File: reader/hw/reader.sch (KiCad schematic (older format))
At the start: 35 parts, among them P101 Wago_233-502, P102 Wago_233-502, P103 CONN_02X05, P104 JST, P105 CONN_01X08, Q101 MMBT2222A, Q102 MMBT2222A, U101 LP2992AIM5-3.3CT-ND, U102 SN75176BDR, U103 MKE04P24M48SF0, X101 CRYSTAL

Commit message: Restructure files and small updates
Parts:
- added R112: R, smd-handsolder:R_1206_HandSoldering, symbol R
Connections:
- wire segments 110 -> 113
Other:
- note added: "PTA3 is open drain output, external pull-up might be\nnecessary see Figure 11-2 in the Kinetis KEO4Z\nuser manual.\n\nBut the input of SN75176 is pulled up internally so\nin this case the resistor is probably not needed. \nSee Figure 19 of TI's sn75176b.pdf\n\nI am keeping the R here just in case it is needed\nfor reliable operation."
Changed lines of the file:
@@
 Text Label 6900 3350 0    60   ~ 0
 IRQ
+$Comp
+L +3.3V #PWR041
+U 1 1 59272043
+P 7000 5000
+F 0 "#PWR041" H 7000 4850 50  0001 C CNN
+F 1 "+3.3V" V 7015 5128 50  0000 L CNN
+F 2 "" H 7000 5000 60  0000 C CNN
+F 3 "" H 7000 5000 60  0000 C CNN
+	1    7000 5000
+	0    -1   -1   0
+$EndComp
+$Comp
+L R R112
+U 1 1 5927213E
+P 7200 5000
+F 0 "R112" V 7300 5000 50  0000 C CNN
+F 1 "R" V 7200 5000 50  0000 C CNN
+F 2 "smd-handsolder:R_1206_HandSoldering" V 7130 5000 30  0001 C CNN
+F 3 "" H 7200 5000 30  0000 C CNN
+	1    7200 5000
+	0    -1   1    0
+$EndComp
+Wire Wire Line
+	7350 5000 7400 5000
+Wire Wire Line
+	7400 5000 7400 4650
+Connection ~ 7400 4650
+Wire Wire Line
+	7000 5000 7050 5000
+Text Notes 5200 6100 0    60   ~ 0
+PTA3 is open drain output, external pull-up might be\nnecessary see Figure 11-2 in the Kinetis KEO4Z\nuser manual.\n\nBut the input of SN75176 is pulled up internally so\nin this case the resistor is probably not needed. \nSee Figure 19 of TI's sn75176b.pdf\n\nI am keeping the R here just in case it is needed\nfor reliable operation.
 $EndSCHEMATC

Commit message: Fix voltage for SPI flash, short under one capacitor
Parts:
- U103: symbol MKE04P24M48SF0 -> MKE04P24M48SF0-RESCUE-reader
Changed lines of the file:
@@
 EESchema Schematic File Version 2
+LIBS:reader-rescue
 LIBS:capacitors
 LIBS:connectors
@@
 $EndDescr
 $Comp
-L MKE04P24M48SF0 U103
+L MKE04P24M48SF0-RESCUE-reader U103
 U 1 1 591A19D8
 P 5850 3950

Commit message: New KiCAD lib references, crystal feedback R, basic uart impl
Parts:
- added R?: 10M, symbol simple:R
- C101, C102, C103, C104, C106, C107, C108, C109, C111: symbol C -> simple:C
- C105, C110: symbol Jamicon_220uF_16V_TKP -> capacitors:Jamicon_220uF_16V_TKP
- D101, D102: symbol LED -> simple:LED
- P101, P102: symbol Wago_233-502 -> connectors:Wago_233-502
- P103: symbol CONN_02X05 -> connectors:CONN_02X05
- P104: symbol CONN_01X02 -> connectors:CONN_01X02
- P105: symbol CONN_01X08 -> connectors:CONN_01X08
- Q101, Q102: symbol MMBT2222A -> transistors:MMBT2222A
- R101, R102, R103, R104, R105, R106, R107, R108, R109, R110, R111, R112: symbol R -> simple:R
- U101: symbol LP2992AIM5-3.3CT-ND -> power:LP2992AIM5-3.3CT-ND
- U102: symbol SN75176BDR -> ic:SN75176BDR
- U103: symbol MKE04P24M48SF0-RESCUE-reader -> reader-rescue:MKE04P24M48SF0-RESCUE-reader
- X101: symbol CRYSTAL -> templates:CRYSTAL

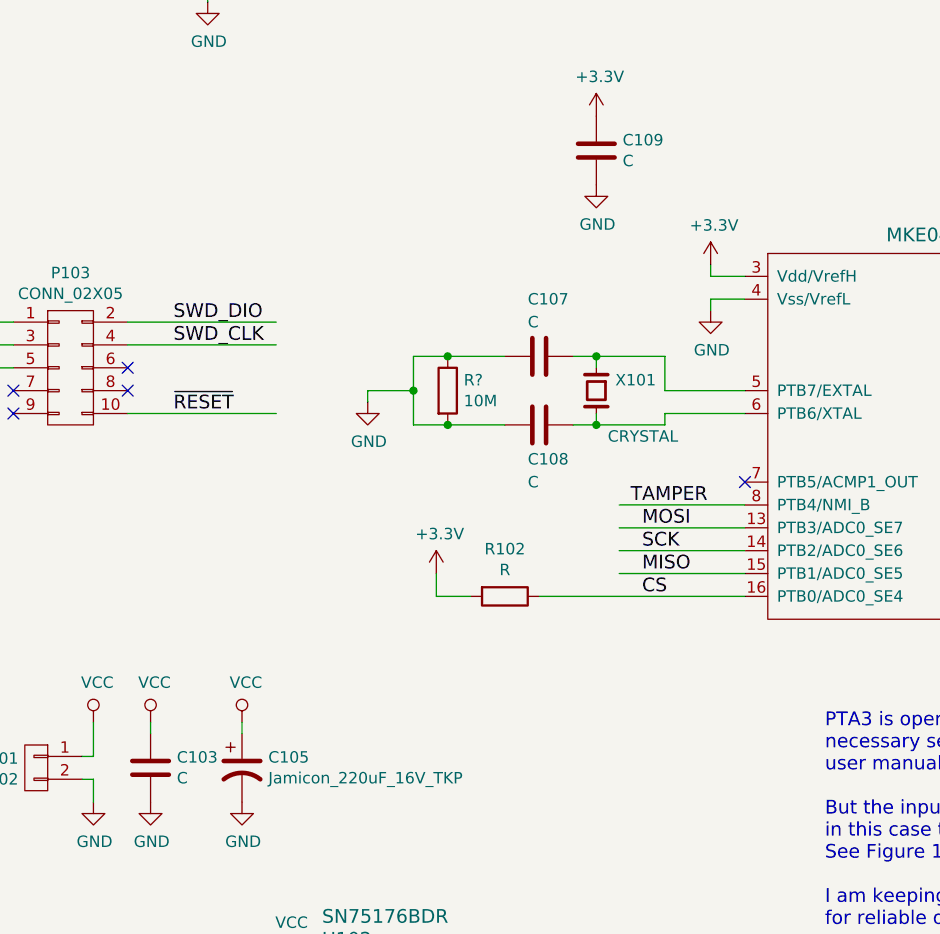
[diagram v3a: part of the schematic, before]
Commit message: Fix MISO/TAMPER issue, fix watchdog, fix corruption when SPI cmd + 1 byte data
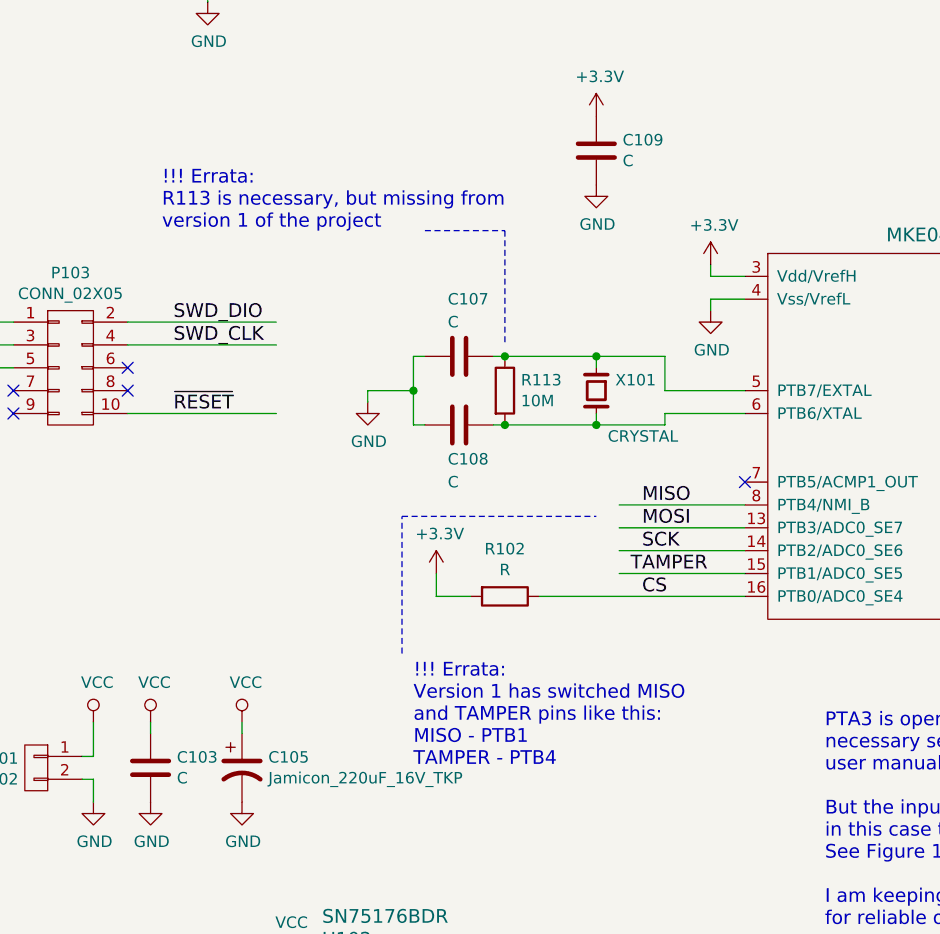
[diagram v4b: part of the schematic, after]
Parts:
- R113: renamed from R?; footprint (none) -> smd-handsolder:R_1206_HandSoldering
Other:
- note added: "!!! Errata:\nR113 is necessary, but missing from\nversion 1 of the project"
- note added: "!!! Errata:\nVersion 1 has switched MISO\nand TAMPER pins like this:\nMISO - PTB1\nTAMPER - PTB4\n"
- moved on the sheet: C107, C108, R113
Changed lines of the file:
@@
 Sheet 1 1
 Title ""
-Date ""
-Rev ""
+Date "2017-11-22"
+Rev "2"
 Comp ""
 Comment1 ""
@@
 Text Label 7000 4550 0    60   ~ 0
 CPU_RX
-Text Label 4400 4550 0    60   ~ 0
+Text Label 4400 4250 0    60   ~ 0
 MISO
 Text Label 4400 4350 0    60   ~ 0
@@
 Wire Wire Line
 	4850 4250 4300 4250
-Text Label 4350 4250 0    60   ~ 0
+Text Label 4350 4550 0    60   ~ 0
 TAMPER
 $Comp
@@
 L simple:C C107
 U 1 1 591E14AD
-P 3950 3600
-F 0 "C107" V 3700 3550 50  0000 L CNN
-F 1 "C" V 3800 3550 50  0000 L CNN
-F 2 "smd-handsolder:C_1206_HandSoldering" H 3988 3450 30  0001 C CNN
-F 3 "" H 3950 3600 60  0000 C CNN
-	1    3950 3600
+P 3600 3600
+F 0 "C107" V 3350 3550 50  0000 L CNN
+F 1 "C" V 3450 3550 50  0000 L CNN
+F 2 "smd-handsolder:C_1206_HandSoldering" H 3638 3450 30  0001 C CNN
+F 3 "" H 3600 3600 60  0000 C CNN
+	1    3600 3600
 	0    1    1    0
 $EndComp
@@
 L simple:C C108
 U 1 1 591E155E
-P 3950 3900
-F 0 "C108" V 4100 3850 50  0000 L CNN
-F 1 "C" V 4200 3850 50  0000 L CNN
-F 2 "smd-handsolder:C_1206_HandSoldering" H 3988 3750 30  0001 C CNN
-F 3 "" H 3950 3900 60  0000 C CNN
-	1    3950 3900
+P 3600 3900
+F 0 "C108" V 3750 3850 50  0000 L CNN
+F 1 "C" V 3850 3850 50  0000 L CNN
+F 2 "smd-handsolder:C_1206_HandSoldering" H 3638 3750 30  0001 C CNN
+F 3 "" H 3600 3900 60  0000 C CNN
+	1    3600 3900
 	0    1    1    0
 $EndComp
@@
 	3400 3600 3400 3900
 Wire Wire Line
-	3400 3600 3800 3600
-Wire Wire Line
-	3400 3900 3800 3900
+	3400 3600 3450 3600
+Wire Wire Line
+	3400 3900 3450 3900
 Connection ~ 3400 3750
 $Comp
@@
 $EndComp
 Wire Wire Line
-	4100 3600 4500 3600
+	3750 3600 4500 3600
 Wire Wire Line
 	4200 3600 4200 3650
 Wire Wire Line
-	4100 3900 4500 3900
+	3750 3900 4500 3900
 Wire Wire Line
 	4200 3900 4200 3850
@@
 PTA3 is open drain output, external pull-up might be\nnecessary see Figure 11-2 in the Kinetis KEO4Z\nuser manual.\n\nBut the input of SN75176 is pulled up internally so\nin this case the resistor is probably not needed. \nSee Figure 19 of TI's sn75176b.pdf\n\nI am keeping the R here just in case it is needed\nfor reliable operation.
 $Comp
-L simple:R R?
+L simple:R R113
 U 1 1 5A10499B
-P 3550 3750
-F 0 "R?" H 3620 3796 50  0000 L CNN
-F 1 "10M" H 3620 3705 50  0000 L CNN
-F 2 "" V 3480 3750 30  0000 C CNN
-F 3 "" H 3550 3750 30  0000 C CNN
-	1    3550 3750
-	1    0    0    -1
-$EndComp
-Connection ~ 3550 3600
-Connection ~ 3550 3900
+P 3800 3750
+F 0 "R113" H 3870 3796 50  0000 L CNN
+F 1 "10M" H 3870 3705 50  0000 L CNN
+F 2 "smd-handsolder:R_1206_HandSoldering" V 3730 3750 30  0001 C CNN
+F 3 "" H 3800 3750 30  0000 C CNN
+	1    3800 3750
+	1    0    0    -1
+$EndComp
+Text Notes 3400 5400 0    60   ~ 0
+!!! Errata:\nVersion 1 has switched MISO\nand TAMPER pins like this:\nMISO - PTB1\nTAMPER - PTB4\n
+Text Notes 2300 3050 0    60   ~ 0
+!!! Errata:\nR113 is necessary, but missing from\nversion 1 of the project
+Wire Notes Line
+	3350 4900 3350 4300
+Wire Notes Line
+	3350 4300 4200 4300
+Connection ~ 3800 3600
+Connection ~ 3800 3900
+Wire Notes Line
+	3450 3050 3800 3050
+Wire Notes Line
+	3800 3050 3800 3550
 $EndSCHEMATC

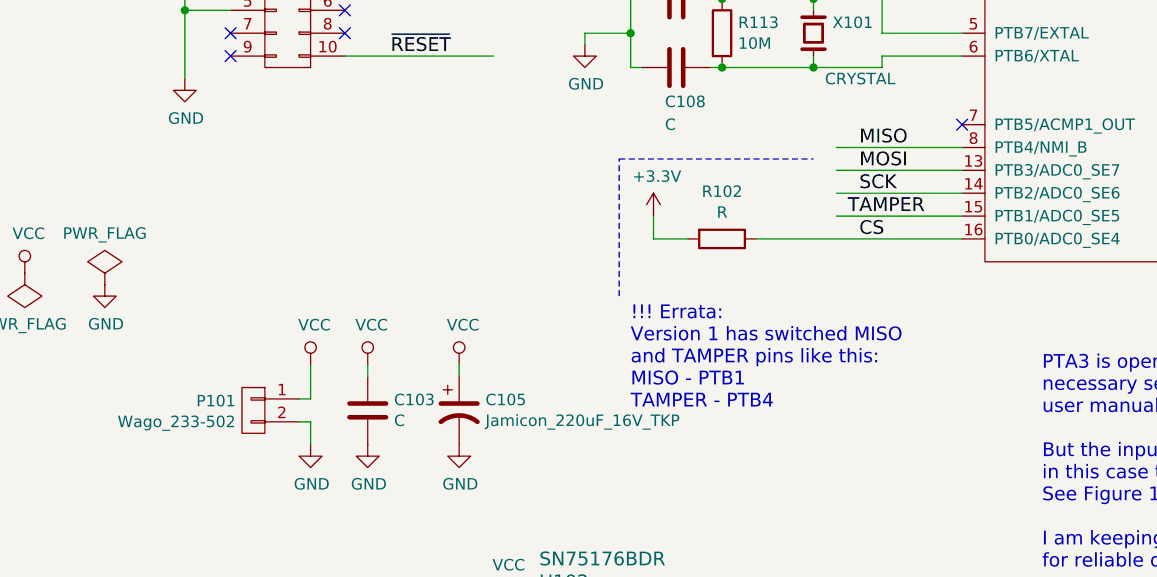
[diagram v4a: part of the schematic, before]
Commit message: Compilability using embc lm4f, fixes to TX_EN switching
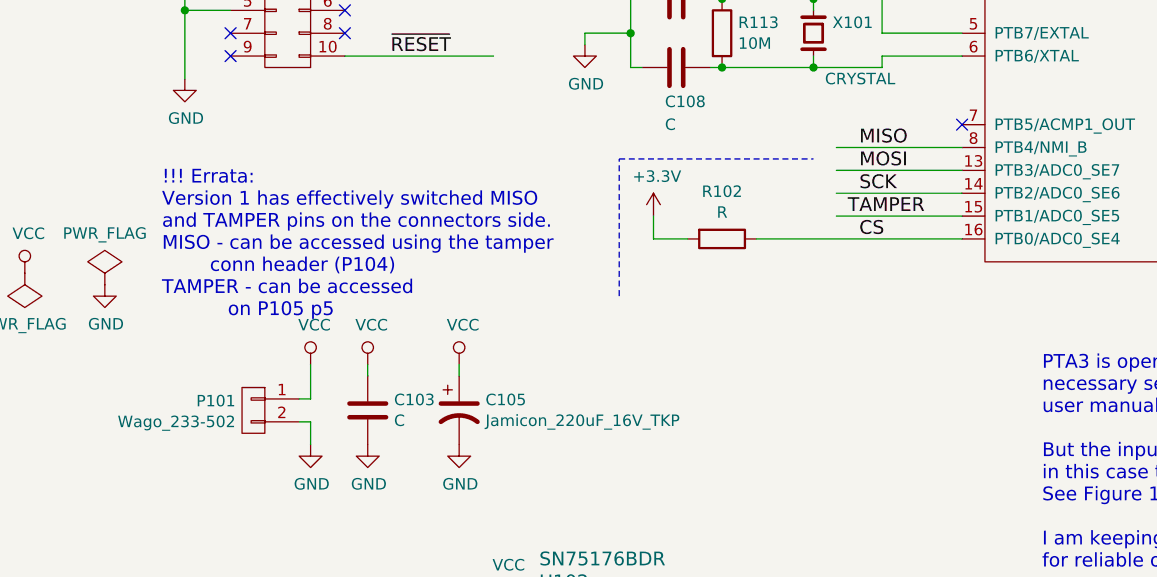
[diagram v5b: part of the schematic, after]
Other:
- note added: "!!! Errata:\nVersion 1 has effectively switched MISO\nand TAMPER pins on the connectors side.\nMISO - can be accessed using the tamper\n conn header (P104)\nTAMPER - can be accessed\n on P105 p5\n"
- note removed: "!!! Errata:\nVersion 1 has switched MISO\nand TAMPER pins like this:\nMISO - PTB1\nTAMPER - PTB4\n"
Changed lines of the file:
@@
 	1    0    0    -1
 $EndComp
-Text Notes 3400 5400 0    60   ~ 0
-!!! Errata:\nVersion 1 has switched MISO\nand TAMPER pins like this:\nMISO - PTB1\nTAMPER - PTB4\n
+Text Notes 1350 5000 0    60   ~ 0
+!!! Errata:\nVersion 1 has effectively switched MISO\nand TAMPER pins on the connectors side.\nMISO - can be accessed using the tamper\n        conn header (P104)\nTAMPER - can be accessed\n           on P105 p5\n
 Text Notes 2300 3050 0    60   ~ 0
 !!! Errata:\nR113 is necessary, but missing from\nversion 1 of the project
